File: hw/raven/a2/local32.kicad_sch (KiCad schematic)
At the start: 93 parts, among them J301 SIMM72, J302 SIMM72, J303 SIMM72, J304 SIMM72, J305 PWM, J306 VUSB, J307 USB2Header, J308 ARGB, J309 ESSI0, J310 ESSI1, J311 DSP_JTAG, U301 CH559L, U302 XR68M752, U303 CH213K, U304 MAX3245CAI+T, U305 DSP56303, U306 AS7C31024B-xxTJ, U307 AS7C31024B-xxTJ, U308 AS7C31024B-xxTJ, U309 SN74LVC1G14DBV, U311 PCM5102A, Y301 ASE-24.000MHZ-L-C-T, Y302 ASELJ-E-22.5792MHz

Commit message: A2: dac + adc + dsp work
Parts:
- added C317, C318, C321: 0.1u, Capacitor_SMD:C_1206_3216Metric_Pad1.33x1.80mm_HandSolder, symbol 68k:c_100nf_smd1206
- added C320: 10u, Capacitor_THT:CP_Radial_D5.0mm_P2.50mm, symbol Device:C_Polarized
- added R344: 33, Resistor_SMD:R_1206_3216Metric_Pad1.30x1.75mm_HandSolder, symbol Device:R
- added U312: PCM180PW, Package_SO:TSSOP-14_4.4x5mm_P0.65mm, symbol 68k:PCM180PW
- J309: renamed from J311; now not fitted; now left out of the parts list
- J310: renamed from J309; now not fitted; now left out of the parts list
- R331: renamed from R335; now not fitted; now left out of the parts list
- renumbered C317 to C319, C318 to C322, C319 to C323, C323 to C324, C324 to C325, C325 to C326, C130 to C327, C321 to C328, C131 to C329, C326 to C330, J310 to J311, R331 to R332, R332 to R333, R333 to R334, R334 to R335, R345 to R336, R336 to R337, R337 to R338, R338 to R339, R339 to R340, R344 to R341, R340 to R342, R341 to R343, U306 to U307, U307 to U308, U308 to U309, U309 to U310
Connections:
- net +3.3V: now also U311.17 (XSMT), C317.2, U312.4 (VDD)
- net +5V: now also C318.1, U312.3 (VCC)
- net DSP_TX: now also J311.10 (Pin_10); no longer J310.10 (Pin_10)
- net ESSI0_SC1: now also U312.7 (LRCK)
- net ESSI0_SCK: now also U312.8 (BCK)
- net ESSI0_SRD: now also U312.9 (DOUT)
- net ESSI1_SC0: now also J311.4 (Pin_4); no longer J311.3 (Pin_3)
- net ESSI1_SCK: now also J311.3 (Pin_3); no longer J311.8 (Pin_8)
- net ESSI1_STD: now also J311.8 (Pin_8); no longer J311.4 (Pin_4)
- net GND: now also C317.1, C318.2, C320.2, C321.1, U312.10 (MD0), U312.11 (MD1), U312.12 (FMT), U312.2 (AGND), U312.5 (DGND)
- net IKBD_DBG_TX: no longer J311.10 (Pin_10)
- net DSP_CLOCK: now reaches U305.55 (EXTAL), Y302.3 (OUTPUT)
- net DSP_CLOCK: now also R344.2
- new net: C320.1, C321.2, U312.1 (VREF)
- new net ADC_CLOCK: R344.1, U312.6 (SCKI)
- new net AUDIO_YM_RAW_L: U312.13 (VINL)
- new net AUDIO_YM_RAW_R: U312.14 (VINR)
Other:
- note added: "A1=LO, A2 = todo: option jumper?"
- note added: "ESSI0 ADC"
- note added: "internal pulldown"
- note added: "same as dsp"
- note added: "slave mode"
- note removed: "A1=LO"
- note removed: "logical physical P 00000-0FFFF 00000-0FFFF Y 00000-0FFFF 00000-0FFFF X 00000-0FFFF 10000-1FFFF DSP_AA0 P,Y,X SRAM_CE1 active low DSP_AA1 X SRAM_A16 active high"
- moved on the sheet: C324, C325, C326, C327, C328, C329, C330, J311, U311, Y302

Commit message: A2 wip
audio hooked up
added caps for fan headers
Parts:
- removed J310: ESSI0, 68k:ESSI-BoxHeader, symbol 68k:ESSI
- removed R301, R343: 10K, Resistor_SMD:R_1206_3216Metric_Pad1.30x1.75mm_HandSolder, symbol Device:R
- removed R338, R339, R340: 1K, Resistor_SMD:R_1206_3216Metric_Pad1.30x1.75mm_HandSolder, symbol Device:R
- added C315, C316, C317, C318, C319, C320, C321, C322, C323, C324, C325, C326: 0.1u, Capacitor_SMD:C_1206_3216Metric_Pad1.33x1.80mm_HandSolder, symbol 68k:c_100nf_smd1206
- added C327, C328, C335, C344: 1u, Capacitor_SMD:C_1206_3216Metric_Pad1.33x1.80mm_HandSolder, symbol 68k:c_100nf_smd1206
- added C515: 10u, Capacitor_THT:CP_Radial_D5.0mm_P2.50mm, symbol Device:C_Polarized
- added C516: 100u, Capacitor_THT:CP_Radial_D5.0mm_P2.50mm, symbol Device:C_Polarized
- J307: Manufacturer_Name (none) -> Wurth Elektronik; Manufacturer_Part_Number (none) -> 61301021121
- J310: renamed from J311; Manufacturer_Name (none) -> Wurth Elektronik; Manufacturer_Name2 (none) -> Wurth Elektronik; Manufacturer_Part_Number2 (none) -> 61301021121; Manufacturer_Part_Numer (none) -> 61201021621
- U303: Manufacturer_Name (none) -> WCH; Manufacturer_Part_Number (none) -> CH213K
- U311: Manufacturer_Name (none) -> Texas Instruments; Manufacturer_Part_Number (none) -> PCM5102APWR
- renumbered C304 to C305, C305 to C306, C306 to C307, C307 to C309, C308 to C310, C309 to C311, C310 to C312, C311 to C313, C312 to C314, C313 to C329, C314 to C330, C315 to C331, C316 to C332, C317 to C333, C318 to C334, C319 to C336, C320 to C337, C321 to C338, C322 to C339, C323 to C340, C324 to C341, C325 to C342, C326 to C343, C327 to C345, C328 to C346, C329 to C347, C330 to C348, R302 to R301, R303 to R302, R304 to R303, R305 to R304, R306 to R305, R307 to R306, R308 to R307, R309 to R308, R310 to R309, R311 to R310, R312 to R311, R313 to R312, R314 to R313, R315 to R314, R316 to R315, R317 to R316, R318 to R317, R319 to R318, R320 to R319, R321 to R320, R322 to R321, R323 to R322, R324 to R323, R325 to R324, R326 to R325, R327 to R326, R328 to R327, R329 to R328, R330 to R329, R331 to R330, R332 to R331, R333 to R332, R334 to R333, R335 to R334, R336 to R335, R337 to R336, R341 to R337, R342 to R338, R344 to R339, U312 to U306
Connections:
- net MODA is gone; now on net +3.3V: U305.137 (*IRQA/MODA)
- net MODB is gone; now on net +3.3V: U305.136 (*IRQB/MODB)
- net MODC is gone; now on net +3.3V: U305.135 (*IRQC/MODC)
- net +12V: now also C515.1
- net +3.3V: now also U305.103 (VCCD), U305.111 (VCCD), U305.119 (VCCD), U305.126 (VCCQ), U305.129 (VCCD), U305.18 (VCCQ), U305.25 (VCCS), U305.38 (VCCH), U305.56 (VCCQ), U305.57 (VCCC), U305.6 (*NMI/PINIT), U305.65 (VCCC), U305.74 (VCCA), U305.8 (VCCS), U305.80 (VCCA), U305.86 (VCCA), U305.91 (VCCQ), U305.95 (VCCA), C315.2, C316.2, C317.2, C318.2, C319.2, C320.2, C321.2, C322.2, C323.2, C324.2, C325.2, C326.2, C327.2, C328.2, C344.1
- net +5V: now also C334.2, C335.2, C516.1; no longer C334.1
- net GND: now also C334.1, C315.1, C316.1, C317.1, C318.1, C319.1, C320.1, C321.1, C322.1, C323.1, C324.1, C325.1, C326.1, C327.1, C328.1, C335.1, C344.2, C515.2, C516.2; no longer C334.2
- no-connect marks 51 -> 47
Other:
- note added: "100uF cap recommended Panasonic EB1A101SH"
- note added: "Datasheet: At least six 0.01-0.1µF caps as close as possible to the four sides of the package. --------- Most sensitive. VCCP/GNDP: 0.47µ as close as possible VCCQ/GNDQ: 0.1µF as close as possible. The rest: VCCA (4 pins) - one 0.1µF VCCD (4 pins) - one 0.1µF VCCC (2 pins) - one 0.1µF VCCH (1 pin, HI08) - one 0.1µF VCCS (2 pins, ESSI/SCI) - one 0.1µF"
- note added: "can remove resistor. but in theory, can be made an ouput from dsp code. safest to keep."
- note added: "if there is room"
- note added: "pullup on uart side uart wakes HIGH"
- note removed: "100uF cap Panasonic EB1A101S"
- moved on the sheet: C334, J305, J308, J310, R336

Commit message: A2: changed oscillator caps
also fixed reference identifier
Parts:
- C314: value 0.1u -> 0.01u; Manufacturer_Part_Number C1206C104K5RACTU -> C1206C103K5RACTU
- C346: value 0.1u -> 0.01u; Manufacturer_Part_Number C1206C104K5RACTU -> C1206C103K5RACTU; Part C1206C104K5RACTU -> C1206C103K5RACTU
- renumbered C515 to C304, C516 to C308, Y301 to X301, Y302 to X302
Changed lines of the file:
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@@
 			)
 		)
-		(property "Value" "0.1u"
+		(property "Value" "0.01u"
 			(at 31.75 304.165 90)
 			(effects
@@
 			)
 		)
-		(property "Manufacturer_Part_Number" "C1206C104K5RACTU"
+		(property "Manufacturer_Part_Number" "C1206C103K5RACTU"
 			(at 48.895 329.565 0)
 			(effects
@@
 		(on_board yes)
 		(dnp no)
-		(property "Reference" "C515"
+		(property "Reference" "C304"
 			(at 437.515 224.155 0)
 			(effects
@@
 			(project "raven"
 				(path "/af55e73e-5814-45b4-ac5c-0bab62c0b1c7/d5022d96-0fa0-4474-b160-b3a99bf8c2e1"
-					(reference "C515")
+					(reference "C304")
 					(unit 1)
 				)
@@
 		(on_board yes)
 		(dnp no)
-		(property "Reference" "C516"
+		(property "Reference" "C308"
 			(at 437.515 246.38 0)
 			(effects
@@
 			(project "raven"
 				(path "/af55e73e-5814-45b4-ac5c-0bab62c0b1c7/d5022d96-0fa0-4474-b160-b3a99bf8c2e1"
-					(reference "C516")
+					(reference "C308")
 					(unit 1)
 				)
@@
 			)
 		)
-		(property "Value" "0.1u"
-			(at 369.57 509.905 90)
+		(property "Value" "0.01u"
+			(at 370.586 510.286 90)
 			(effects
 				(font
@@
 			)
 		)
-		(property "Part" "C1206C104K5RACTU"
+		(property "Part" "C1206C103K5RACTU"
 			(at 352.425 535.305 0)
 			(effects
@@
 			)
 		)
-		(property "Manufacturer_Part_Number" "C1206C104K5RACTU"
+		(property "Manufacturer_Part_Number" "C1206C103K5RACTU"
 			(at 372.745 507.365 0)
 			(effects
@@
 		(on_board yes)
 		(dnp no)
-		(property "Reference" "Y301"
+		(property "Reference" "X301"
 			(at 34.798 314.96 0)
 			(effects
@@
 			(project ""
 				(path "/af55e73e-5814-45b4-ac5c-0bab62c0b1c7/d5022d96-0fa0-4474-b160-b3a99bf8c2e1"
-					(reference "Y301")
+					(reference "X301")
 					(unit 1)
 				)
@@
 		(on_board yes)
 		(dnp no)
-		(property "Reference" "#PWR0458"
+		(property "Reference" "#PWR0337"
 			(at 436.88 259.715 0)
 			(effects
@@
 			(project "raven"
 				(path "/af55e73e-5814-45b4-ac5c-0bab62c0b1c7/d5022d96-0fa0-4474-b160-b3a99bf8c2e1"
-					(reference "#PWR0458")
+					(reference "#PWR0337")
 					(unit 1)
 				)
@@
 		(on_board yes)
 		(dnp no)
-		(property "Reference" "Y302"
+		(property "Reference" "X302"
 			(at 389.128 503.428 0)
 			(effects
@@
 			(project ""
 				(path "/af55e73e-5814-45b4-ac5c-0bab62c0b1c7/d5022d96-0fa0-4474-b160-b3a99bf8c2e1"
-					(reference "Y302")
+					(reference "X302")
 					(unit 1)
 				)

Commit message: misc a2 work
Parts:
- removed C301: 0.1u, Capacitor_SMD:C_1206_3216Metric_Pad1.33x1.80mm_HandSolder, symbol 68k:c_100nf_smd1206
- removed C306: 10u, Capacitor_SMD:C_1206_3216Metric_Pad1.33x1.80mm_HandSolder, symbol 68k:c_100nf_smd1206
- removed J306: VUSB, Jumper:SolderJumper-2_P1.3mm_Open_RoundedPad1.0x1.5mm, symbol Jumper:SolderJumper_2_Open
- removed J309: DSP_JTAG, 68k:SAMTEC_FTSH-105-01-L-D-K, symbol 68k:JTAG small - FTSH-105-01-L-D-K
- removed R301: 10K, Resistor_SMD:R_1206_3216Metric_Pad1.30x1.75mm_HandSolder, symbol Device:R
- removed R307, R308, R309, R310, R311, R319, R320, R321, R322, R323: 470, Resistor_SMD:R_1206_3216Metric_Pad1.30x1.75mm_HandSolder, symbol Device:R
- removed R330: 220, Resistor_SMD:R_1206_3216Metric_Pad1.30x1.75mm_HandSolder, symbol Device:R
- added D301: PMEG2010ER, 68k:SOD-123W-handsolder, symbol Diode:PMEG2010ER
- added TP301, TP302: TestPoint, TestPoint:TestPoint_Pad_D1.0mm, symbol Connector:TestPoint
- C302: renamed from C307; now left out of the parts list
- U302: renamed from U303; now left out of the parts list
- X301: footprint ASE24576MHZLCT -> 68k:ASE24576MHZLCT
- X302: footprint ASELJE225792MHzLRT -> 68k:ASELJE225792MHzLRT
- renumbered C302 to C301, C305 to C303, C303 to C304, C304 to C305, C308 to C306, C309 to C307, C310 to C308, C311 to C309, C312 to C310, C313 to C311, C314 to C312, C315 to C313, C316 to C314, C317 to C315, C318 to C316, C319 to C317, C320 to C318, C321 to C319, C322 to C320, C323 to C321, C324 to C322, C325 to C323, C326 to C324, C327 to C325, C328 to C326, C329 to C327, C330 to C328, C331 to C329, C332 to C330, C333 to C331, C334 to C332, C335 to C333, C336 to C334, C337 to C335, C338 to C336, C339 to C337, C340 to C338, C341 to C339, C342 to C340, C343 to C341, C344 to C342, C345 to C343, C346 to C344, C347 to C345, C348 to C346, J307 to J306, J308 to J307, J310 to J308, R302 to R301, R303 to R302, R304 to R303, R305 to R304, R306 to R305, R312 to R306, R313 to R307, R314 to R308, R315 to R309, R316 to R310, R317 to R311, R318 to R312, R324 to R313, R326 to R314, R327 to R315, R328 to R316, R329 to R317, R331 to R318, R332 to R319, R333 to R320, R334 to R321, R335 to R322, R336 to R323, R325 to R324, R337 to R325, R338 to R326, R339 to R327, U302 to U303
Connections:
- net COM1:CD is gone; now on net GND: U304.4 (R1IN)
- net COM1:DSR is gone; now on net GND: U304.5 (R2IN)
- net COM1:RI is gone; now on net GND: U304.8 (R5IN)
- net DSP_JTAG_CLK is gone; now on net +3.3V: U305.141 (TCK)
- net J0BTN1 is gone; now on net JOY0:BTN1: R305.2, U301.6 (LED3/TNOW_/TXD1_/DA4/P4.4)
- net J0DOWN is gone; now on net JOY0:DOWN: R302.2, U301.19 (DA1/P4.1)
- net J0LEFT is gone; now on net JOY0:LEFT: R303.2, U301.15 (PWM3_/CAP3_/DA2/P4.2), U301.9 (LED1/!A15/INT1/P3.3)
- net J0RIGHT is gone; now on net JOY0:RIGHT: R304.2, U301.14 (PWM1_/DA3/P4.3)
- net J0UP is gone; now on net JOY0:UP: R301.2, U301.20 (LED2/RXD1_/DA0/P4.0), U301.8 (LED0/INT0/P3.2)
- net J1BTN1 is gone; now on net JOY0:BTN2: R310.2, U301.25 (P2.4/A12/PWM1), U301.5 (PWM2_/DA5/P4.5)
- net J1DOWN is gone; now on net JOY1:DOWN: R307.2, U301.22 (P2.1/A9/MOSI1)
- net J1LEFT is gone; now on net JOY1:LEFT: R308.2, U301.23 (P2.2/A10/MISO1)
- net J1RIGHT is gone; now on net JOY1:RIGHT: R309.2, U301.24 (P2.3/A11/SCK1)
- net J1UP is gone; now on net JOY1:UP: R306.2, U301.21 (P2.0/A8)
- net +5V: now also D301.2 (A)
- net IKBD_DBG_TX: now also TP302.1
- net VUSB: now also D301.1 (K)
- net ~{DSP_RESET}: now also U305.138 (*TRST)
- net ~{CKBD_BL}: now reaches U301.16 (XI/SCS_/P4.6)
- net ~{CKBD_BL}: now also TP301.1
- net DSP_A16: no longer names the net of U305.98 (A16)
- net DSP_A17: no longer names the net of U305.99 (A17)
- net DSP_JTAG_TDI: no longer names the net of U305.140 (TDI)
- net DSP_JTAG_TMO: no longer names the net of U305.139 (TDO)
- net DSP_JTAG_TMS: no longer names the net of U305.142 (TMS)
- net ~{DSP_JTAG_DE}: no longer names the net of U305.5 (*DE)
- no-connect marks 47 -> 51
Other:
- note added: "1A 0.3V drop"
- note added: "VCCP"
- note added: "do not change, datasheet insist on 0.47u pair with GNDP (47)"
- note removed: "custom"
- note removed: "do not change, datasheet insist on 0.47u"
- note removed: "pullup on uart side uart wakes HIGH"
- note removed: "static mcr inputs pwr_sw jumpers (failsafe mode jumper?)"
- moved on the sheet: C302, C303, R324, U302

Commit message: A2 routing
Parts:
- removed TP301, TP302: TestPoint, TestPoint:TestPoint_Pad_D1.0mm, symbol Connector:TestPoint
- added R301, R307: 10K, Resistor_SMD:R_1206_3216Metric_Pad1.30x1.75mm_HandSolder, symbol Device:R
- renumbered R301 to R302, R302 to R303, R303 to R304, R304 to R305, R305 to R306, R306 to R308, R307 to R309, R308 to R310, R309 to R311, R310 to R312, R311 to R313, R312 to R314, R313 to R315, R314 to R316, R315 to R317, R316 to R318, R317 to R319, R318 to R320, R319 to R321, R320 to R322, R321 to R323, R322 to R324, R323 to R325, R324 to R326, R325 to R327, R326 to R328, R327 to R329
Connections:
- net +3.3V: now also R301.1, R307.1
- net IKBD_DBG_TX: now also R301.2
- net ~{CKBD_BL}: now also R307.2

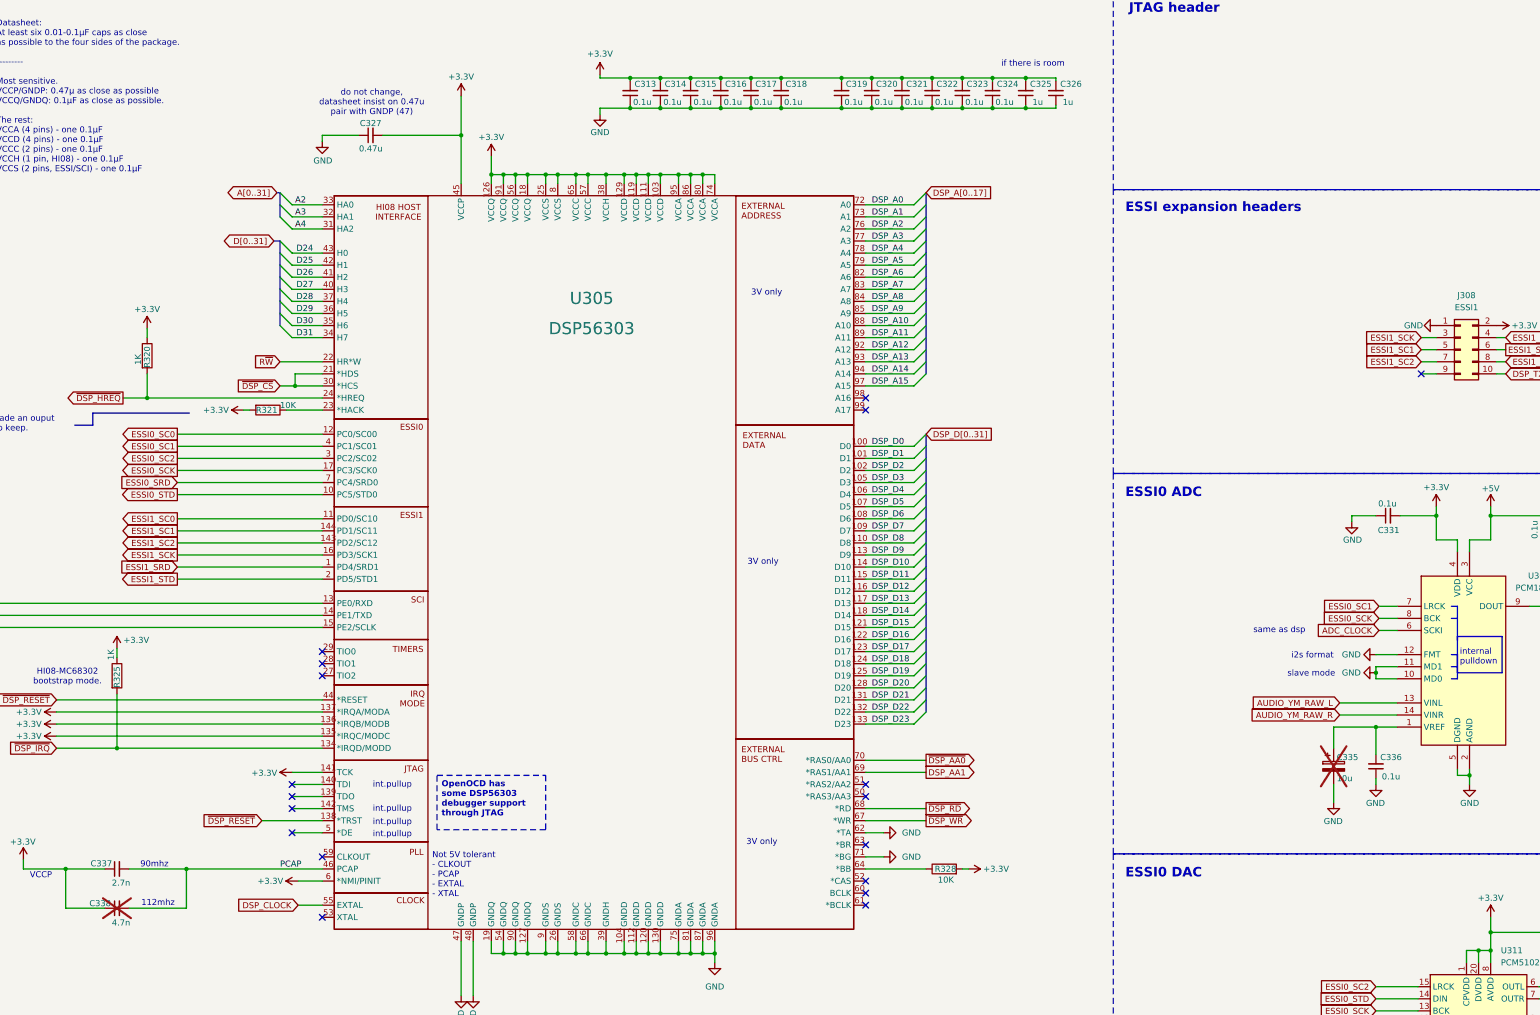
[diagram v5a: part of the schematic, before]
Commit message: A2: schema + routing complete. ERC + DRC complete.
Let sit for a while, revisit and sanity check with fresh eyes before gerber.
Todo: double check BOM export and fix missing infos if any.
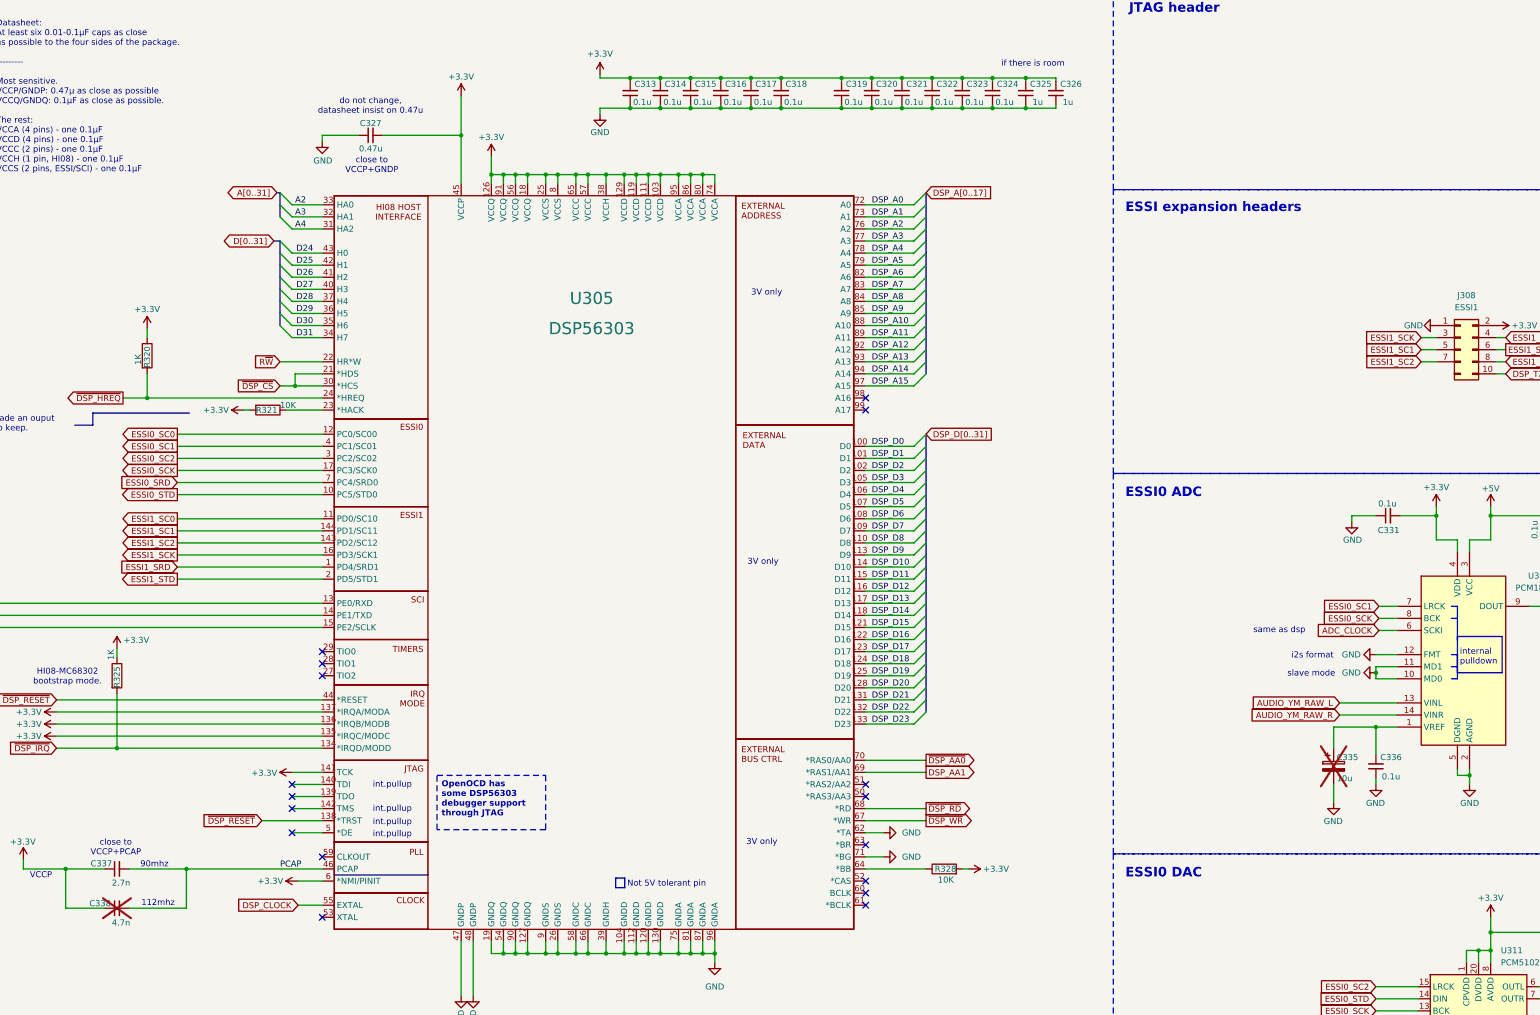
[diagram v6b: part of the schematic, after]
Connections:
- no-connect marks 51 -> 50
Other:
- note added: "close to VCCP+GNDP"
- note added: "close to VCCP+PCAP"
- note added: "do not change, datasheet insist on 0.47u"
- note removed: "Not 5V tolerant - CLKOUT - PCAP - EXTAL - XTAL"
- note removed: "do not change, datasheet insist on 0.47u pair with GNDP (47)"
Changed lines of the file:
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@@
 	)
 	(rectangle
+		(start 501.65 471.805)
+		(end 521.335 479.425)
+		(stroke
+			(width 0)
+			(type solid)
+		)
+		(fill
+			(type color)
+			(color 255 236 0 0.25)
+		)
+	)
+	(rectangle
 		(start 451.485 165.735)
 		(end 453.39 167.767)
@@
 	)
 	(rectangle
+		(start 560.832 468.63)
+		(end 562.737 470.662)
+		(stroke
+			(width 0)
+			(type solid)
+		)
+		(fill
+			(type color)
+			(color 255 242 0 0.25)
+		)
+	)
+	(rectangle
 		(start 514.35 36.83)
 		(end 586.105 59.055)
@@
 	)
 	(rectangle
+		(start 586.105 373.38)
+		(end 610.87 439.42)
+		(stroke
+			(width 0)
+			(type solid)
+		)
+		(fill
+			(type color)
+			(color 255 236 0 0.25)
+		)
+	)
+	(rectangle
 		(start 144.78 209.55)
 		(end 173.99 231.14)
@@
 	)
 	(rectangle
+		(start 586.105 439.42)
+		(end 610.87 479.425)
+		(stroke
+			(width 0)
+			(type solid)
+		)
+		(fill
+			(type color)
+			(color 255 236 0 0.25)
+		)
+	)
+	(rectangle
+		(start 501.65 461.01)
+		(end 521.335 467.995)
+		(stroke
+			(width 0)
+			(type solid)
+		)
+		(fill
+			(type color)
+			(color 255 236 0 0.25)
+		)
+	)
+	(rectangle
+		(start 586.105 325.12)
+		(end 610.87 373.38)
+		(stroke
+			(width 0)
+			(type solid)
+		)
+		(fill
+			(type color)
+			(color 255 236 0 0.25)
+		)
+	)
+	(rectangle
 		(start 483.235 201.93)
 		(end 544.83 269.24)
@@
 		)
 	)
+	(text "close to\nVCCP+PCAP"
+		(exclude_from_sim no)
+		(at 455.676 462.28 0)
+		(effects
+			(font
+				(size 1.27 1.27)
+			)
+		)
+	)
 	(text "AutoShutdownPlus Disabled\n\nFORCEON = ~{FORCEOFF} = VCC, no load\n\nT_OUT = Always active\nR_OUT = Always active\nT_IN = has no pullups"
 		(exclude_from_sim no)
@@
 		)
 	)
-	(text "Not 5V tolerant\n- CLKOUT\n- PCAP\n- EXTAL\n- XTAL"
-		(exclude_from_sim no)
-		(at 522.224 467.995 0)
-		(effects
-			(font
-				(size 1.27 1.27)
-			)
-			(justify left)
-		)
-	)
 	(text "0 = mute\n1 = unmute"
 		(exclude_from_sim no)
@@
 		)
 	)
+	(text "close to\nVCCP+GNDP"
+		(exclude_from_sim no)
+		(at 509.524 318.77 0)
+		(effects
+			(font
+				(size 1.27 1.27)
+			)
+		)
+	)
 	(text "3V only"
 		(exclude_from_sim no)
@@
 		)
 	)
-	(text "do not change,\ndatasheet insist on 0.47u\npair with GNDP (47)"
+	(text "do not change,\ndatasheet insist on 0.47u"
 		(exclude_from_sim no)
-		(at 509.524 305.562 0)
+		(at 509.27 306.324 0)
 		(effects
 			(font
@@
 		)
 	)
+	(text "Not 5V tolerant pin"
+		(exclude_from_sim no)
+		(at 563.245 469.9 0)
+		(effects
+			(font
+				(size 1.27 1.27)
+			)
+			(justify left)
+		)
+	)
 	(text "i/o connector"
 		(exclude_from_sim no)
@@
 	)
 	(no_connect
-		(at 730.25 362.585)
-	)
-	(no_connect
 		(at 534.67 109.855)
 	)
@@
 	(wire
 		(pts
-			(xy 730.25 362.585) (xy 733.425 362.585)
-		)
-		(stroke
-			(width 0)
-			(type default)
-		)
-	)
-	(wire
-		(pts
 			(xy 266.7 278.765) (xy 273.685 278.765)
 		)
@@
 	)
 	(symbol
-		(lib_name "SIMM72-Raven_1")
 		(lib_id "68k:SIMM72-Raven")
 		(at 64.135 106.68 0)
@@
 	)
 	(symbol
-		(lib_name "SIMM72-Raven_2")
 		(lib_id "68k:SIMM72-Raven")
 		(at 127.635 106.68 0)
@@
 	)
 	(symbol
-		(lib_name "SIMM72-Raven_3")
 		(lib_id "68k:SIMM72-Raven")
 		(at 187.96 106.68 0)
@@
 			)
 		)
-		(pin "9"
-		)
 		(pin "10"
 		)
@@
 		(at 711.835 445.135 0)
 		(unit 1)
-		(exclude_from_sim no)
+		(exclude_from_sim yes)
 		(in_bom no)
 		(on_board no)
